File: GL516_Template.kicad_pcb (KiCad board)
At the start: 2 copper layers, 315.8 x 99.2 mm, 90 parts, among them J10 Conn_01x01, J11 Conn_01x01, J12 Conn_01x01, J13 Conn_01x01, J14 Conn_01x01, J15 Conn_01x01, J16 Conn_01x01, J17 Conn_01x01, J2 Conn_01x01, J3 Conn_01x01, J4 Conn_01x01, J5 Conn_01x01, J6 Conn_01x01, J7 Conn_01x01, J8 Conn_01x01, J9 Conn_01x01, SW1 SW_PUSH, SW2 KEY_SWITCH, SW3 SW_PUSH, SW4 KEY_SWITCH, SW4 SW_PUSH, SW5 SW_PUSH, SW7 SW_PUSH, SW8 SW_PUSH

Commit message: Alice with TrackBall TopPlate Create
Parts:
- removed the SW4 at (292.9, 57.1)
- removed the SW4 at (271.5, 66.7)
- removed the SW4 at (233.4, 66.7)
- removed the SW4 at (238.1, 28.6)
- removed the SW4 at (214.3, 66.7)
- removed the SW4 at (161.9, 28.6)
- removed the SW4 at (176.2, 66.7)
- removed the SW4 at (181.0, 28.6)
- removed the SW4 at (200.0, 28.6)
- removed the SW4 at (195.3, 66.7)
- removed the SW4 at (142.9, 28.6)
- removed the SW4 at (38.1, 85.7)
- removed the SW4 at (138.1, 66.7)
- removed the SW4 at (123.8, 28.6)
- removed the SW4 at (157.2, 66.7)
- removed the SW4 at (119.1, 66.7)
- removed the SW4 at (104.8, 28.6)
- removed the SW4 at (100.0, 66.7)
- removed the SW4 at (85.7, 28.6)
- removed the SW4 at (81.0, 66.7)
- removed the SW4 at (66.7, 28.6)
- removed the SW4 at (61.9, 66.7)
- removed the SW4 at (276.2, 28.6)
- removed the SW4 at (47.6, 28.6)
- removed the SW4 at (295.3, 28.6)
- removed the SW4 at (314.3, 66.7)
- removed the SW4 at (252.4, 66.7)
- removed the SW4 at (219.1, 28.6)
- removed the SW4 at (257.2, 28.6)
- removed the SW5 at (245.3, 104.8)
- removed the SW5 at (221.5, 104.8)
- removed the SW5 at (178.6, 104.8)
- removed the SW5 at (116.7, 104.8)
- removed the SW7 at (31.0, 104.8)
- removed the SW7 at (73.8, 104.8)
- removed the SW7 at (52.4, 104.8)
- removed the SW8 at (200.0, 104.8)
- removed the SW8 at (266.7, 47.6)
- removed the SW8 at (247.7, 47.6)
- removed the SW8 at (228.6, 47.6)
- removed the SW8 at (238.1, 85.7)
- removed the SW8 at (257.2, 85.7)
- removed the SW8 at (276.2, 85.7)
- removed the SW8 at (190.5, 47.6)
- removed the SW8 at (171.4, 47.6)
- removed the SW8 at (200.0, 85.7)
- removed the SW8 at (219.1, 85.7)
- removed the SW8 at (138.1, 104.8)
- removed the SW8 at (209.6, 47.6)
- removed the SW8 at (181.0, 85.7)
- removed the SW8 at (123.8, 85.7)
- removed the SW8 at (152.4, 47.6)
- removed the SW8 at (142.9, 85.7)
- removed the SW8 at (133.3, 47.6)
- removed the SW8 at (161.9, 85.7)
- removed the SW8 at (114.3, 47.6)
- removed the SW8 at (95.2, 104.8)
- removed the SW8 at (104.8, 85.7)
- removed the SW8 at (157.2, 104.8)
- removed the SW8 at (95.2, 47.6)
- removed the SW8 at (85.7, 85.7)
- removed the SW8 at (76.2, 47.6)
- removed the SW8 at (66.7, 85.7)
- removed the SW8 at (57.1, 47.6)
- removed the SW8 at (295.3, 104.8)
- removed the SW8 at (314.3, 104.8)
- removed the SW8 at (276.2, 104.8)
- removed the SW8 at (295.3, 85.7)
- removed the SW8 at (314.3, 47.6)
- removed the SW8 at (314.3, 85.7)
- added SW10: S, kbd_SW_Hole:SW_Hole, F.Cu at (76.2, 47.7)
- added SW11: D, kbd_SW_Hole:SW_Hole, F.Cu at (95.1, 50.4)
- added SW12: F, kbd_SW_Hole:SW_Hole, F.Cu at (114.0, 53.0)
- added SW13: G, kbd_SW_Hole:SW_Hole, F.Cu at (132.9, 55.7)
- added SW14: =, kbd_SW_Hole:SW_Hole, F.Cu at (151.8, 58.3)
- added SW15: Shift, kbd_SW_Hole:SW_Hole_1.75, F.Cu at (35.7, 66.8)
- added SW16: Z, kbd_SW_Hole:SW_Hole, F.Cu at (62.0, 66.8)
- added SW17: X, kbd_SW_Hole:SW_Hole, F.Cu at (83.0, 67.9)
- added SW18: C, kbd_SW_Hole:SW_Hole, F.Cu at (101.9, 70.6)
- added SW19: V, kbd_SW_Hole:SW_Hole, F.Cu at (120.8, 73.3)
- added SW20: B, kbd_SW_Hole:SW_Hole, F.Cu at (139.7, 75.9)
- added SW21: Alt, kbd_SW_Hole:SW_Hole_1.25, F.Cu at (87.4, 87.8)
- added SW22: Fn1, kbd_SW_Hole:SW_Hole_1.25, F.Cu at (111.1, 91.2)
- added SW23: Space, kbd_SW_Hole:SW_Hole_1.25, F.Cu at (134.7, 94.5)
- added SW24: L_Click, kbd_SW_Hole:SW_Hole_1.25, F.Cu at (164.9, 105.8)
- added SW25: Y, kbd_SW_Hole:SW_Hole, F.Cu at (193.1, 38.8)
- added SW26: U, kbd_SW_Hole:SW_Hole, F.Cu at (212.0, 36.1)
- added SW27: I, kbd_SW_Hole:SW_Hole, F.Cu at (230.9, 33.4)
- added SW28: O, kbd_SW_Hole:SW_Hole, F.Cu at (249.8, 30.8)
- added SW29: P, kbd_SW_Hole:SW_Hole, F.Cu at (268.7, 28.1)
- added SW30: [, kbd_SW_Hole:SW_Hole, F.Cu at (295.2, 28.6)
- added SW32: H, kbd_SW_Hole:SW_Hole, F.Cu at (200.5, 57.0)
- added SW33: J, kbd_SW_Hole:SW_Hole, F.Cu at (219.4, 54.3)
- added SW34: K, kbd_SW_Hole:SW_Hole, F.Cu at (238.3, 51.7)
- added SW35: L, kbd_SW_Hole:SW_Hole, F.Cu at (257.2, 49.0)
- added SW36: ;, kbd_SW_Hole:SW_Hole, F.Cu at (276.1, 46.4)
- added SW37: ', kbd_SW_Hole:SW_Hole, F.Cu at (299.9, 47.7)
- added SW38: N, kbd_SW_Hole:SW_Hole, F.Cu at (212.6, 74.6)
- added SW39: M, kbd_SW_Hole:SW_Hole, F.Cu at (231.5, 71.9)
- added SW4: E, kbd_SW_Hole:SW_Hole, F.Cu at (93.0, 30.8)
- added SW40: <, kbd_SW_Hole:SW_Hole, F.Cu at (250.4, 69.3)
- added SW41: >, kbd_SW_Hole:SW_Hole, F.Cu at (269.3, 66.6)
- added SW42: /, kbd_SW_Hole:SW_Hole, F.Cu at (295.2, 66.8)
- added SW43: \, kbd_SW_Hole:SW_Hole, F.Cu at (314.3, 66.8)
- added SW44: R_Click, kbd_SW_Hole:SW_Hole_1.25, F.Cu at (188.7, 105.8)
- added SW45: Enter, kbd_SW_Hole:SW_Hole_1.25, F.Cu at (217.6, 93.2)
- added SW46: Fn2, kbd_SW_Hole:SW_Hole_1.25, F.Cu at (241.2, 89.9)
- added SW47: BackSpace, kbd_SW_Hole:SW_Hole_1.25, F.Cu at (264.9, 86.5)
- added SW5: R, kbd_SW_Hole:SW_Hole, F.Cu at (111.9, 33.4)
- added SW6: T, kbd_SW_Hole:SW_Hole, F.Cu at (130.9, 36.1)
- added SW7: -, kbd_SW_Hole:SW_Hole, F.Cu at (149.8, 38.7)
- added SW8: Ctrl, kbd_SW_Hole:SW_Hole_1.25, F.Cu at (31.0, 47.7)
- added SW9: A, kbd_SW_Hole:SW_Hole, F.Cu at (52.5, 47.7)
- SW1: value SW_PUSH -> GESC
- SW2: value KEY_SWITCH -> Q; footprint kbd_SW_Hole:SW_Hole_1.5 -> kbd_SW_Hole:SW_Hole
- SW3: value SW_PUSH -> W; footprint kbd_SW_Hole:SW_Hole_1.75 -> kbd_SW_Hole:SW_Hole
- SW31: renamed from SW4; value SW_PUSH -> ]
- moved SW3 54.4 mm to (74.1, 28.1), turned to 352 degrees
- moved SW2 23.8 mm to (47.7, 28.6)
- moved SW31 0.05 mm to (314.3, 28.6)
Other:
- outline, holes or cut-outs redrawn

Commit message: 外形線をオリジナルに合わせて変更
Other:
- board size 315.8 x 99.2 mm -> 314.4 x 98.8 mm
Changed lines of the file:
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@@
   (gr_line (start 323.825 20.05) (end 323.825 113.25) (layer F.Fab) (width 0.1))
   (gr_line (start 19.075 20.05) (end 19.075 113.25) (layer F.Fab) (width 0.1))
-  (gr_arc (start 16.575 113.25) (end 13.575 113.25) (angle -90) (layer Edge.Cuts) (width 0.1))
-  (gr_arc (start 16.575 20.05) (end 16.575 17.05) (angle -90) (layer Edge.Cuts) (width 0.1))
-  (gr_arc (start 326.325 20.05) (end 329.325 20.05) (angle -90) (layer Edge.Cuts) (width 0.1))
-  (gr_arc (start 326.325 113.25) (end 326.325 116.25) (angle -90) (layer Edge.Cuts) (width 0.1))
-  (gr_line (start 329.325 113.25) (end 329.325 20.05) (layer Edge.Cuts) (width 0.1))
-  (gr_line (start 16.575 116.25) (end 326.325 116.25) (layer Edge.Cuts) (width 0.1))
-  (gr_line (start 13.575 20.05) (end 13.575 113.25) (layer Edge.Cuts) (width 0.1))
-  (gr_line (start 326.325 17.05) (end 16.575 17.05) (layer Edge.Cuts) (width 0.1))
+  (gr_arc (start 17.275 113.05) (end 14.275 113.05) (angle -90) (layer Edge.Cuts) (width 0.1))
+  (gr_arc (start 17.275 20.25) (end 17.275 17.25) (angle -90) (layer Edge.Cuts) (width 0.1))
+  (gr_arc (start 325.625 20.25) (end 328.625 20.25) (angle -90) (layer Edge.Cuts) (width 0.1))
+  (gr_arc (start 325.625 113.05) (end 325.625 116.05) (angle -90) (layer Edge.Cuts) (width 0.1))
+  (gr_line (start 328.625 113.05) (end 328.625 20.25) (layer Edge.Cuts) (width 0.1))
+  (gr_line (start 17.275 116.05) (end 325.625 116.05) (layer Edge.Cuts) (width 0.1))
+  (gr_line (start 14.275 20.25) (end 14.275 113.05) (layer Edge.Cuts) (width 0.1))
+  (gr_line (start 325.625 17.25) (end 17.275 17.25) (layer Edge.Cuts) (width 0.1))
 )

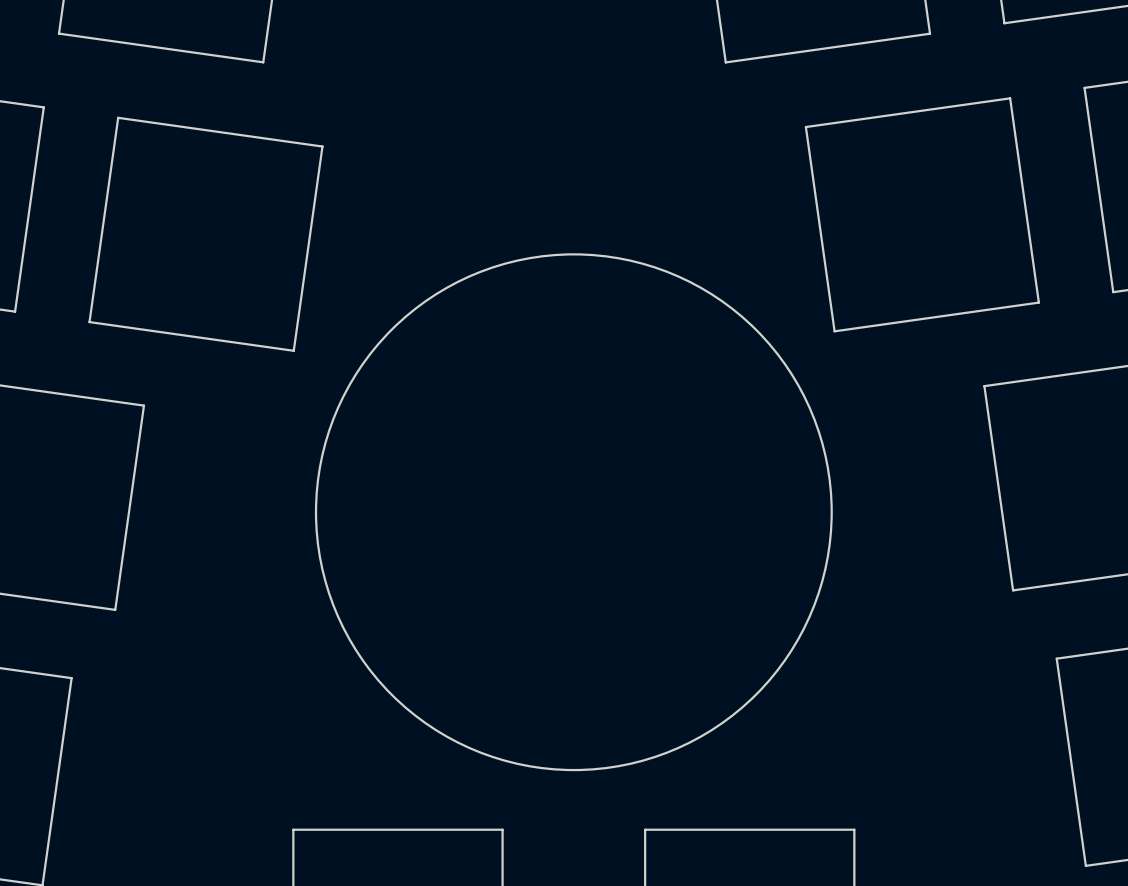
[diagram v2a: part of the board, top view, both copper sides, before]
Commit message: トラックボール穴位置調整
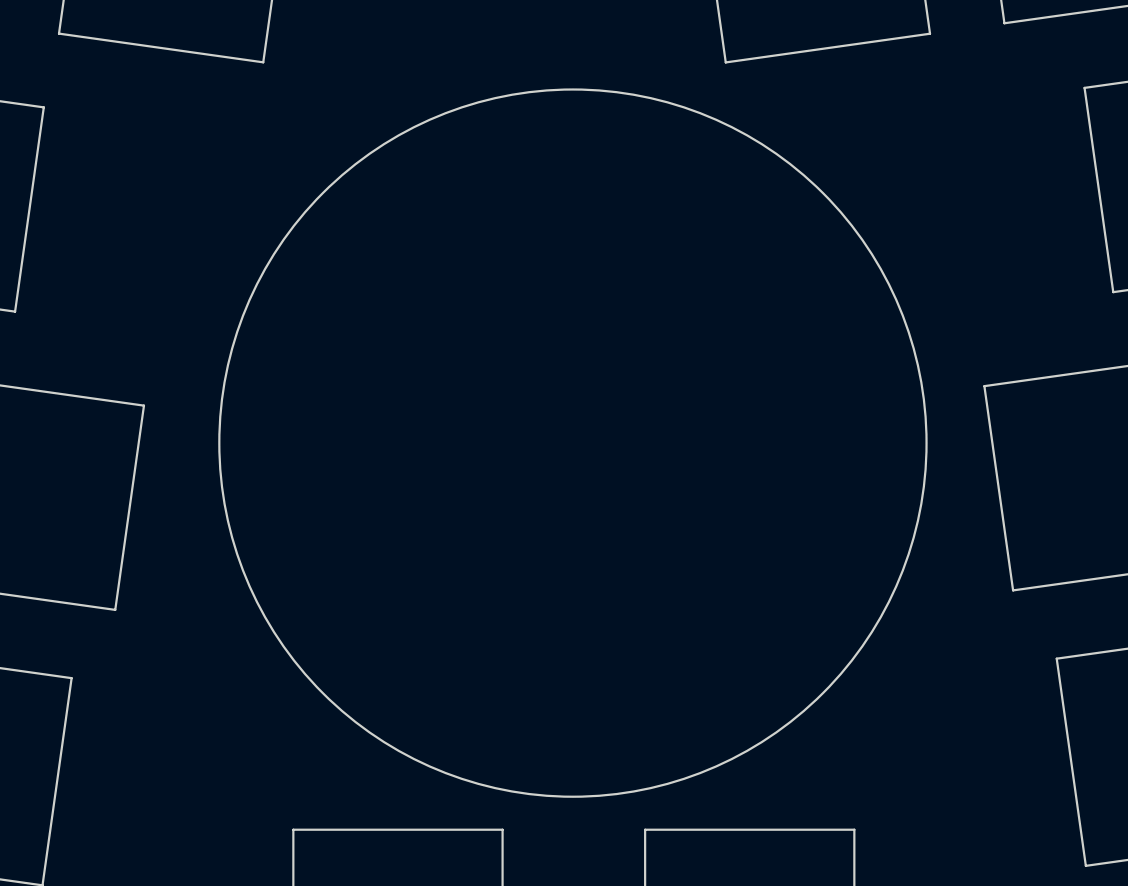
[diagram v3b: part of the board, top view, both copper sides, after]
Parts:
- removed the SW14 at (151.8, 58.3)
- removed the SW21 at (87.4, 87.8)
- removed the SW30 at (295.2, 28.6)
- removed the SW42 at (295.2, 66.8)
- removed SW46: Fn2, kbd_SW_Hole:SW_Hole_1.25
- removed SW47: BackSpace, kbd_SW_Hole:SW_Hole_1.25
- added SW16: X, kbd_SW_Hole:SW_Hole, F.Cu at (83.0, 67.9)
- added SW24: ], kbd_SW_Hole:SW_Hole, F.Cu at (193.1, 38.8)
- added SW31: H, kbd_SW_Hole:SW_Hole, F.Cu at (219.4, 54.3)
- added SW44: TAB/Fn2, kbd_SW_Hole:SW_Hole_1.25, F.Cu at (241.2, 89.9)
- SW17: value X -> C
- SW18: value C -> V
- SW19: value V -> B
- SW20: value B -> Alt; footprint kbd_SW_Hole:SW_Hole -> kbd_SW_Hole:SW_Hole_1.25
- SW30: renamed from SW31; value ] -> -
- SW32: value H -> J
- SW33: value J -> K
- SW34: value K -> L
- SW35: value L -> ;
- SW36: value ; -> '
- SW37: value ' -> N
- SW38: value N -> M
- SW39: value M -> ,
- SW40: value < -> .
- SW41: value > -> /
- SW43: value \ -> Enter; footprint kbd_SW_Hole:SW_Hole -> kbd_SW_Hole:SW_Hole_1.25
- SW45: value Enter -> BackSpace
- SW7: value - -> [
- moved SW43 100.2 mm to (217.6, 93.2), turned to 8 degrees
- moved SW37 72.6 mm to (231.5, 71.9), turned to 8 degrees
- moved SW36 69.5 mm to (212.6, 74.6)
- moved SW20 53.7 mm to (87.4, 87.8)
- moved SW45 47.7 mm to (264.9, 86.5)
- moved SW41 45.0 mm to (314.3, 66.8), turned to 0 degrees
- moved SW40 44.8 mm to (295.2, 66.8), turned to 0 degrees
- moved SW35 42.8 mm to (299.9, 47.7), turned to 0 degrees
- moved SW34 38.2 mm to (276.1, 46.4)
- moved SW39 38.2 mm to (269.3, 66.6)
- moved SW33 38.2 mm to (257.2, 49.0)
- moved SW38 38.2 mm to (250.4, 69.3)
- moved SW32 38.2 mm to (238.3, 51.7)
- moved SW29 26.4 mm to (295.2, 28.6), turned to 0 degrees
- moved SW17 19.1 mm to (101.9, 70.6)
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- renumbered SW15 to SW14, SW16 to SW15, SW22 to SW21, SW23 to SW22, SW24 to SW23, SW44 to SW42
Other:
- outline, holes or cut-outs redrawn
